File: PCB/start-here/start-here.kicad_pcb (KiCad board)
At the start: 4 copper layers, 100 x 60 mm, 50 parts, among them J1 USB_C_Receptacle_PowerOnly_6P, J2 Conn_ARM_SWD_TagConnect_TC2030, J3 RJ45_Hanrun_HR911105A_Horizon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, U1 AP7361C-33E, U2 STM32F439ZITx, U3 LAN8742A, Y1 Crystal_GND24

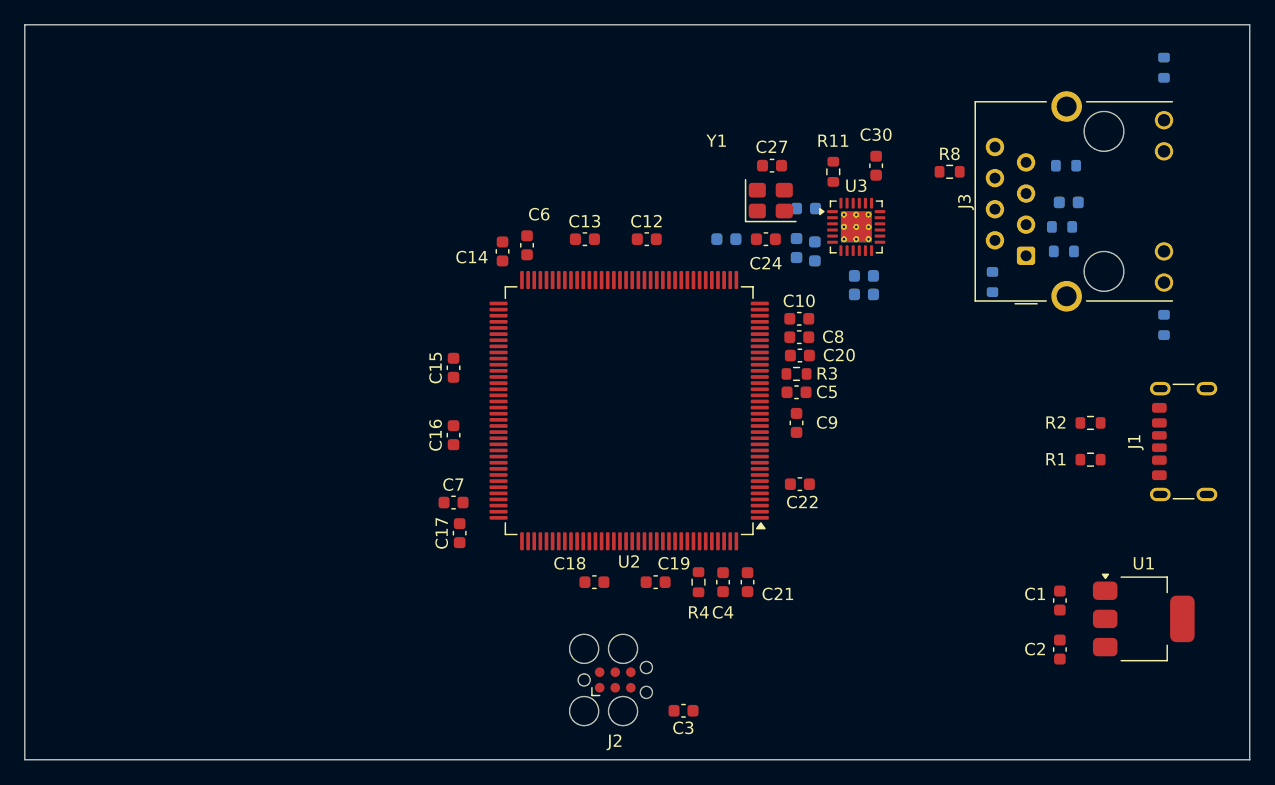
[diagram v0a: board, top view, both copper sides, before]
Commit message: routed PCB, DRC violations present
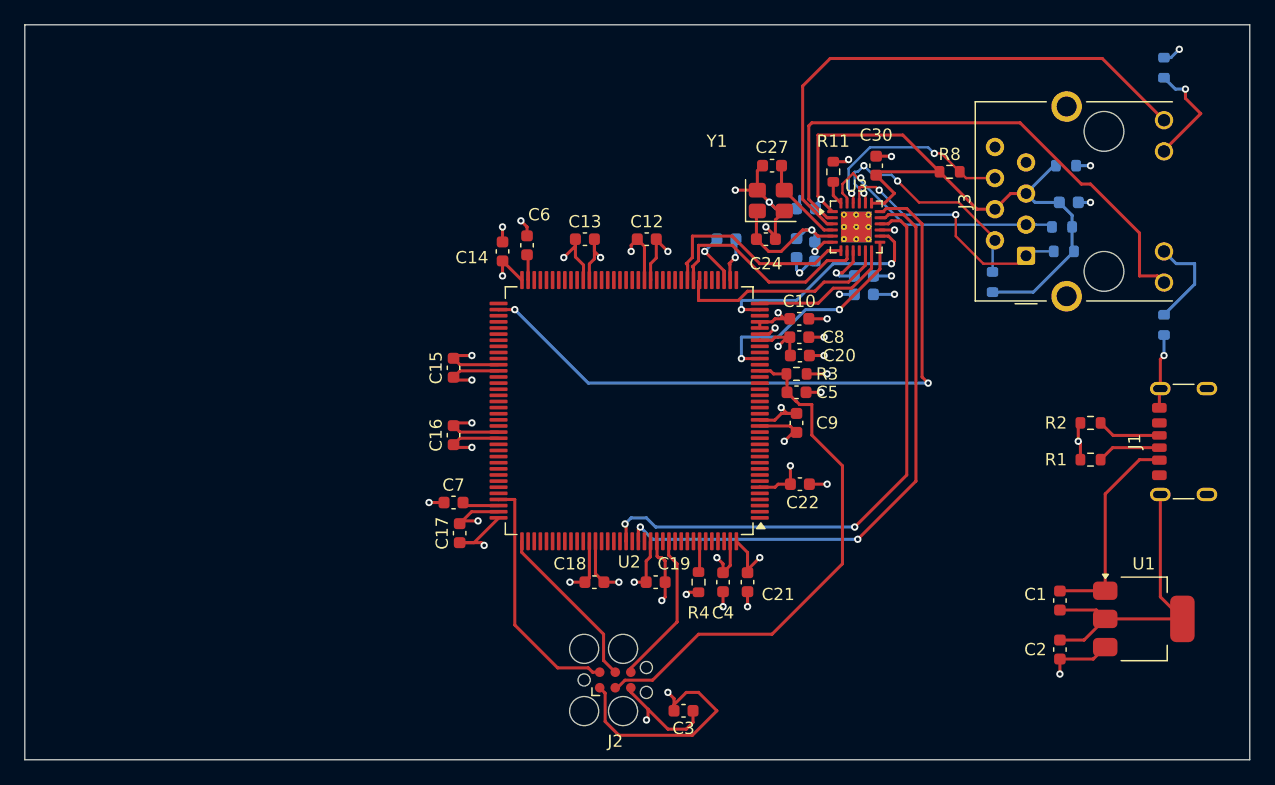
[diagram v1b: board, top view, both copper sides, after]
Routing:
- net GND: track 0.00 -> 128.4 mm, vias 0 -> 34
- net +3.3V: track 0.00 -> 107.6 mm, vias 0 -> 22
- net PHY_VDDA: track 0.00 -> 56.2 mm, vias 0 -> 1
- net TXD1: track 0.00 -> 54.8 mm, vias 0 -> 2
- net TXD0: track 0.00 -> 50.3 mm, vias 0 -> 2
- net TXEN: track 0.00 -> 49.5 mm, vias 0 -> 2
- net LED2: track 0.00 -> 45.1 mm
- net LED1: track 0.00 -> 45.0 mm
- net NRST: track 0.00 -> 43.0 mm
- net RXP: track 0.00 -> 21.9 mm, vias 0 -> 1
- net TXP: track 0.00 -> 21.2 mm, vias 0 -> 2
- net SWDIO: track 0.00 -> 20.1 mm
- net TXN: track 0.00 -> 19.9 mm, vias 0 -> 3
- net MDC: track 0.00 -> 19.1 mm, vias 0 -> 2
- net REF_CLK: track 0.00 -> 19.0 mm, vias 0 -> 2
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
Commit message: resize PCB and pour polygons
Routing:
- added copper zone on B.Cu, net GND
- added copper zone on F.Cu, net GND
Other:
- board size 100 x 60 mm -> 80 x 60 mm
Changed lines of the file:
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@@
 	)
 	(gr_line
-		(start 60 40)
-		(end 60 100)
+		(start 80 40)
+		(end 80 100)
 		(stroke
 			(width 0.05)
@@
 	)
 	(gr_line
-		(start 60 40)
+		(start 80 40)
 		(end 160 40)
 		(stroke
@@
 	(gr_line
 		(start 160 100)
-		(end 60 100)
+		(end 80 100)
 		(stroke
 			(width 0.05)
@@
 	)
 	(zone
+		(net 1)
+		(net_name "GND")
+		(layer "F.Cu")
+		(hatch edge 0.5)
+		(priority 2)
+		(connect_pads
+			(clearance 0.5)
+		)
+		(min_thickness 0.25)
+		(filled_areas_thickness no)
+		(fill yes
+			(thermal_gap 0.5)
+			(thermal_bridge_width 0.5)
+		)
+		(polygon
+			(pts
+				(xy 80 40) (xy 160 40) (xy 160 100) (xy 80 100)
+			)
+		)
+	)
+	(zone
+		(net 1)
+		(net_name "GND")
+		(layer "B.Cu")
+		(hatch edge 0.5)
+		(priority 3)
+		(connect_pads
+			(clearance 0.5)
+		)
+		(min_thickness 0.25)
+		(filled_areas_thickness no)
+		(fill yes
+			(thermal_gap 0.5)
+			(thermal_bridge_width 0.5)
+		)
+		(polygon
+			(pts
+				(xy 80 40) (xy 160 40) (xy 160 100) (xy 80 100)
+			)
+		)
+	)
+	(zone
 		(net 3)
 		(net_name "+3.3V")
 		(layer "In1.Cu")
 		(hatch edge 0.5)
-		(priority 1)
 		(connect_pads
 			(clearance 0.5)
@@
 		(polygon
 			(pts
-				(xy 60 40) (xy 160 40) (xy 160 100) (xy 60 100)
+				(xy 80 40) (xy 160 40) (xy 160 100) (xy 80 100)
 			)
 		)
@@
 		(layer "In2.Cu")
 		(hatch edge 0.5)
+		(priority 1)
 		(connect_pads
 			(clearance 0.5)
@@
 		(polygon
 			(pts
-				(xy 58.5 38.5) (xy 162 39) (xy 161 102.5) (xy 57 102.5)
+				(xy 80 40) (xy 160 40) (xy 160 100) (xy 80 100)
 			)
 		)
